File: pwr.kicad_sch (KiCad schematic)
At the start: 52 parts, among them U1 STM32N657X0H3Q

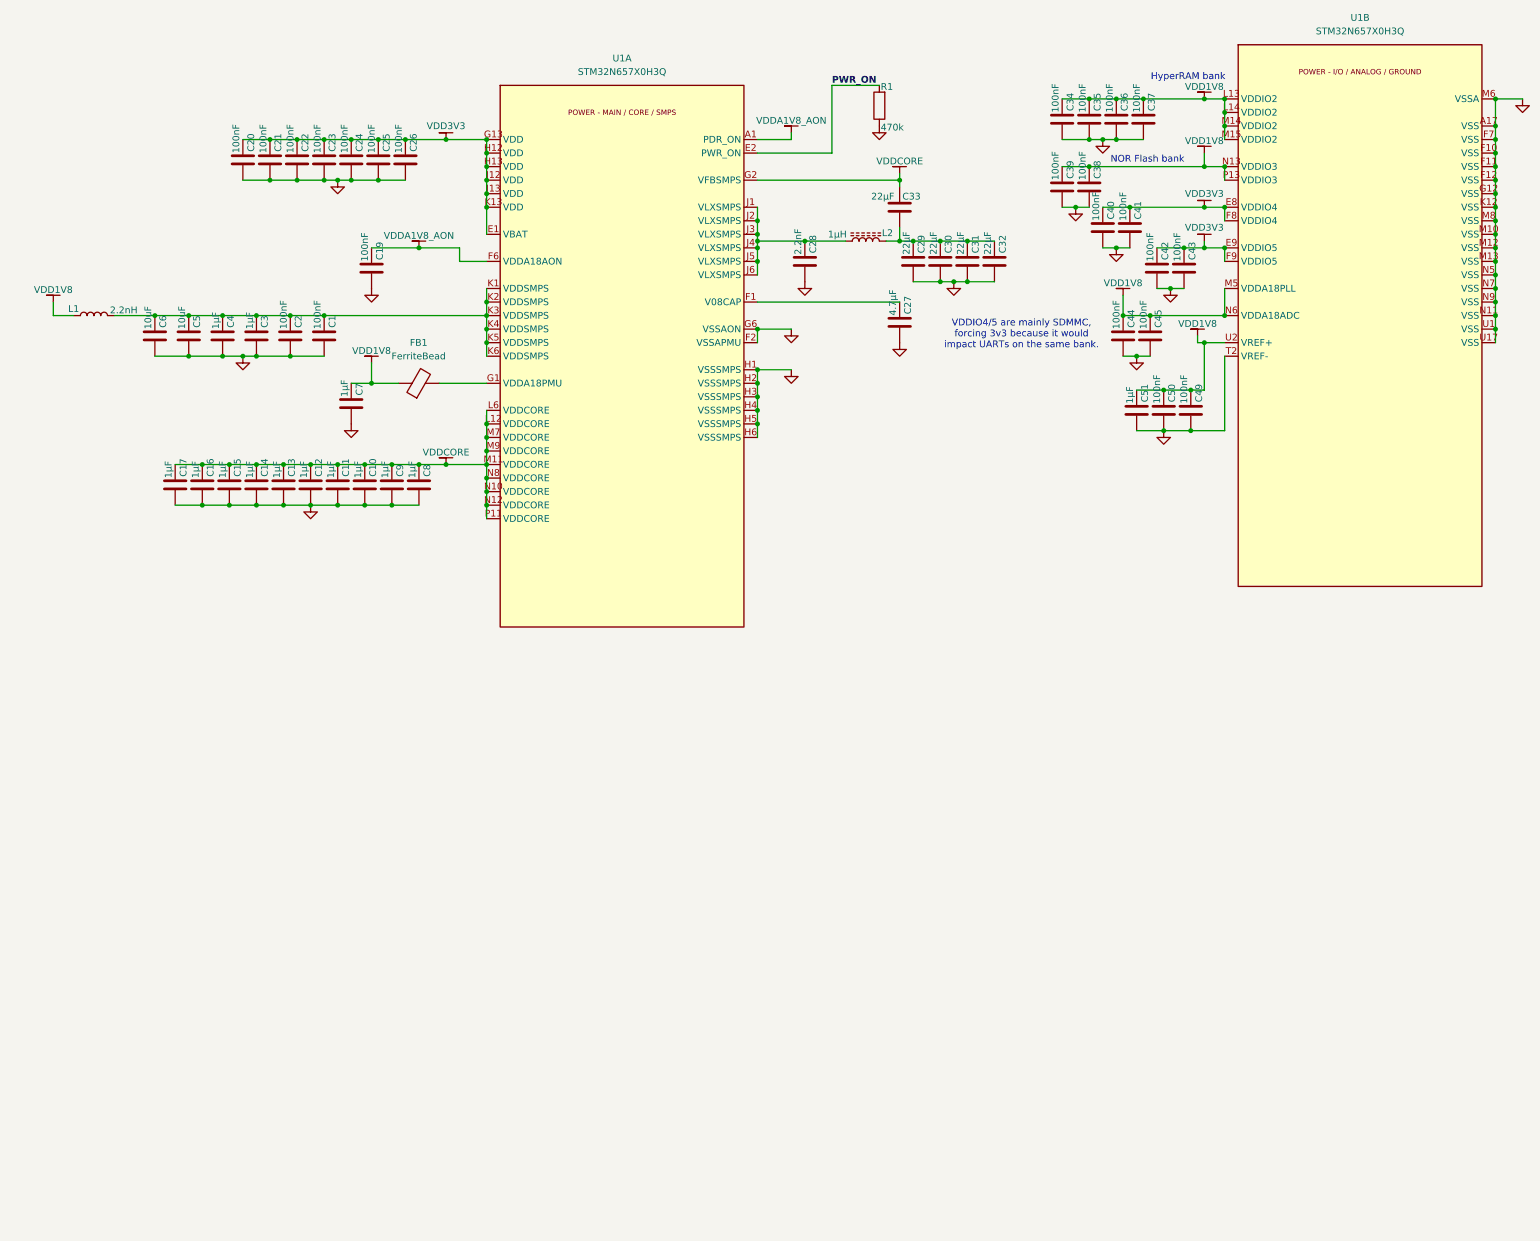
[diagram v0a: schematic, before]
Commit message: Power should be OK, memory & clk routing WIP
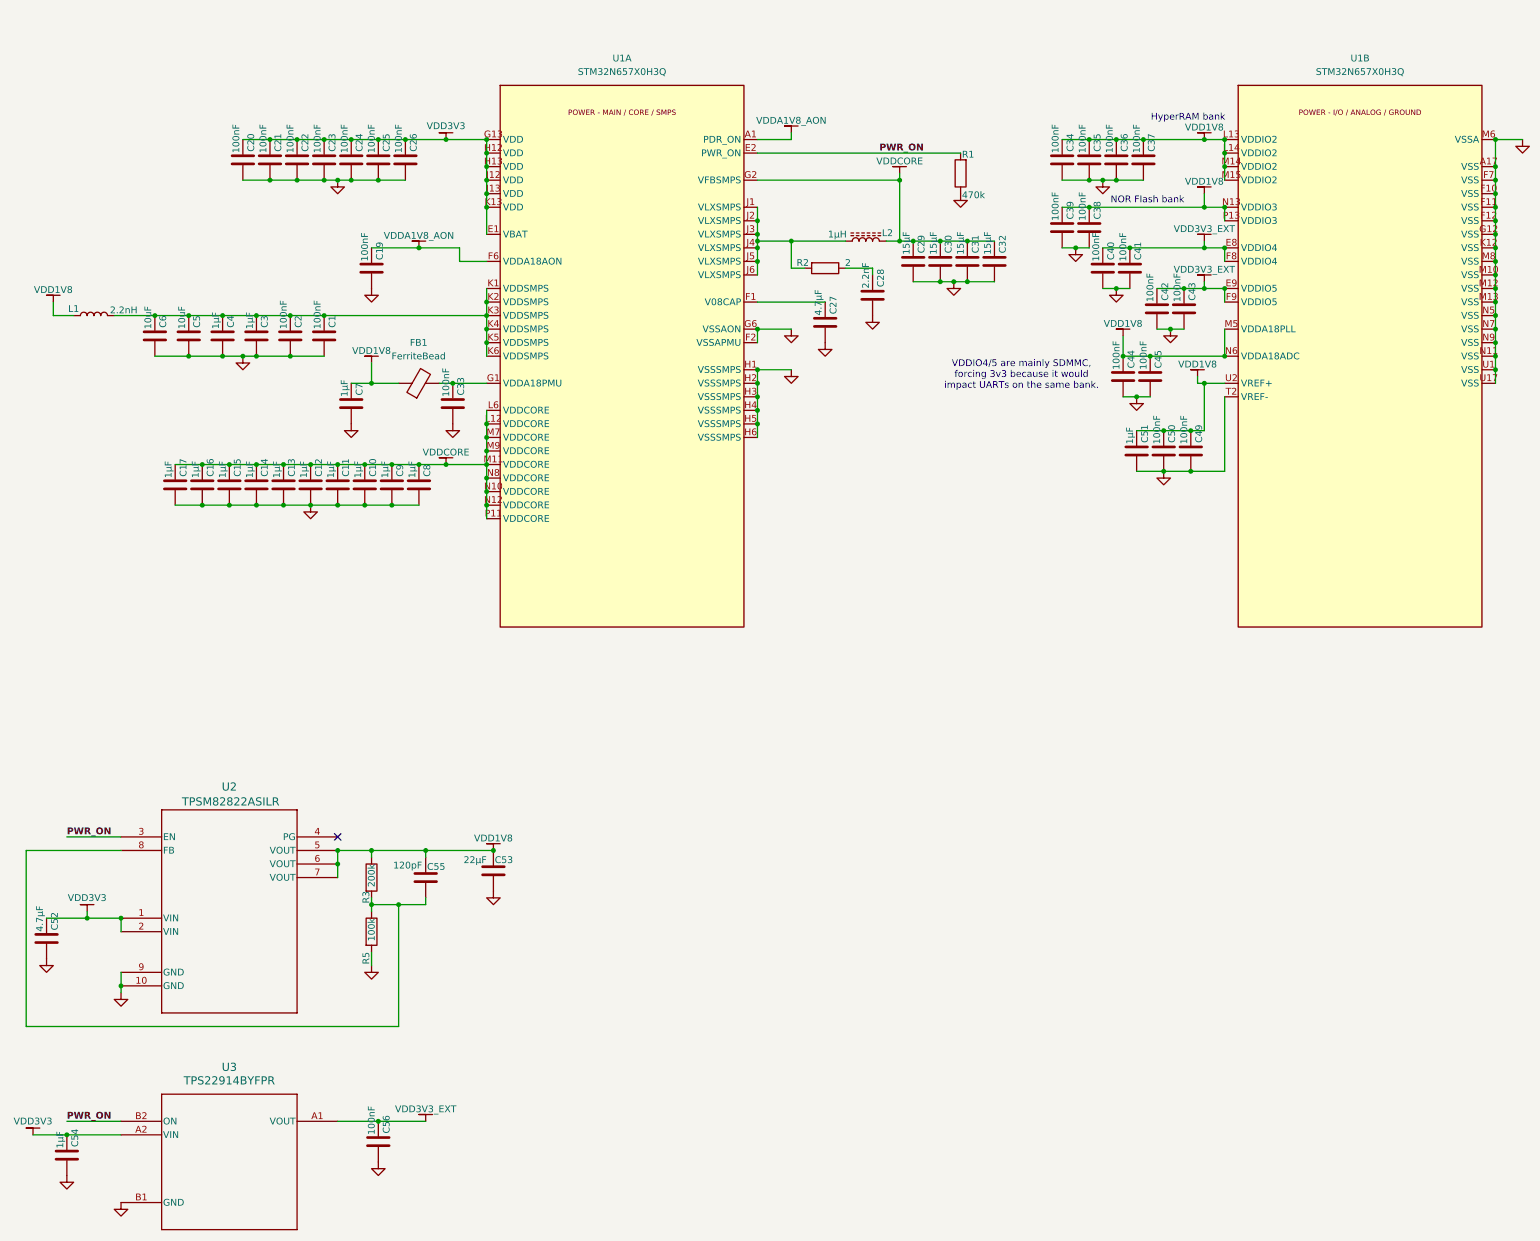
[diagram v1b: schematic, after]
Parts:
- added C52: 4.7µF, symbol Device:C
- added C53: 22µF, symbol Device:C
- added C54: 1µF, symbol Device:C
- added C55: 120pF, symbol Device:C
- added C56: 100nF, symbol Device:C
- added R2: 2, symbol Device:R
- added R3: 200k, symbol Device:R
- added R5: 100k, symbol Device:R
- added U2: TPSM82822ASILR, PLib:SIL0010D_TEX, symbol PLib:TPSM82822ASILR
- added U3: TPS22914BYFPR, PLib:YFP4_TEX, symbol PLib:TPS22914BYFPR
- C29, C30, C31, C32: value 22µF -> 15µF
- C33: value 22µF -> 100nF
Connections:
- net GND: now also C33.2, C52.2, C53.2, C54.2, C56.2, R5.2, U2.10 (GND), U2.9 (GND), U3.B1 (GND)
- net PWR_ON: now also U2.3 (EN), U3.B2 (ON)
- net VDD1V8: now also C53.1, C55.1, R3.1, U2.5 (VOUT), U2.6 (VOUT), U2.7 (VOUT)
- net VDD3V3: now also C52.1, C54.1, U2.1 (VIN), U2.2 (VIN), U3.A2 (VIN); no longer C40.1, C41.1, C42.1, C43.1, U1.E8 (VDDIO4), U1.E9 (VDDIO5), U1.F8 (VDDIO4), U1.F9 (VDDIO5)
- net VDDCORE: now also C29.1, C30.1, C31.1, C32.1, L2.2; no longer C33.1
- net at FB1.2, U1.G1 (VDDA18PMU): now also C33.1
- net at L2.1, U1.J1 (VLXSMPS), U1.J2 (VLXSMPS)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: now also R2.2; no longer C28.1
- new net: C55.2, R3.2, R5.1, U2.8 (FB)
- new net: C28.1, R2.1
- new net VDD3V3_EXT: C40.1, C41.1, C42.1, C43.1, C56.1, U1.E8 (VDDIO4), U1.E9 (VDDIO5), U1.F8 (VDDIO4), U1.F9 (VDDIO5), U3.A1 (VOUT)
- no-connect marks 0 -> 1
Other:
- moved on the sheet: C27, C34, C35, C36, C37, C38, C39, C40, C41, C42, C43, C44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

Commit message: Lots of footprint & memory schematic
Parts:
- removed C1, C42, C43, C44, C45, C49, C50: 100nF, symbol Device:C
- removed C10, C11, C12, C13, C14, C15, C16, C7, C8, C9: 1µF, symbol Device:C
- added C69, C70, C71, C72, C73, C74, C75, C76, C77, C78, C79, C80, C81, C82, C83: 100nF, Capacitor_SMD:C_0201_0603Metric, symbol Device:C
- C17, C2, C20, C21, C22, C23, C24, C25, C26, C4, C51: footprint (none) -> Capacitor_SMD:C_0201_0603Metric
- C19: value 100nF -> 10uF; footprint (none) -> Capacitor_SMD:C_0402_1005Metric
- C27, C28, C54, C56, C6: footprint (none) -> Capacitor_SMD:C_0402_1005Metric
- C29, C30, C31, C32, C52, C53, C55, FB1, L1: footprint (none) -> Capacitor_SMD:C_0603_1608Metric
- C3: value 1µF -> 100nF; footprint (none) -> Capacitor_SMD:C_0201_0603Metric
- C33, C34, C35, C36, C37, C38, C39, C40, C41: value 100nF -> 1µF; footprint (none) -> Capacitor_SMD:C_0201_0603Metric
- C5: value 10uF -> 1µF; footprint (none) -> Capacitor_SMD:C_0201_0603Metric
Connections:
- net GND: now also C69.2, C70.2, C71.2, C72.2, C73.2, C74.2, C75.2, C76.2, C77.2, C78.2, C79.2, C80.2, C81.2, C82.2, C83.2
- net VDD1V8: now also C71.1, C72.1, C73.1, C74.1, C75.1, C76.1, C81.1, C82.1, C83.1; no longer C34.1, C35.1, C36.1, C37.1, C38.1, C39.1
- net VDD3V3_EXT: now also C77.1, C78.1, C79.1, C80.1; no longer C40.1, C41.1
- net VDDA1V8_AON: now also C69.1; no longer C19.1
- net VDDCORE: now also C33.1, C34.1, C35.1, C36.1, C37.1, C38.1, C39.1, C40.1, C41.1
- net at C2.1, C3.1, C4.1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: now also C19.1
- net at FB1.2, U1.G1 (VDDA18PMU): now also C70.1; no longer C33.1
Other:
- note added: "VDDIO2 bank: PO[5:0] and PP[15:0] VDDIO3 bank: PN[12:0]"

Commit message: Power & memory should be ok, sanity check in progress, routing started (routing first then GPIO set for mezzanine)
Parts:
- added C57, C58: 1µF, Capacitor_SMD:C_0402_1005Metric, symbol Device:C
- added U6: (no value), PLib:DQN_X2SON4_1mmx1mm, symbol PLib:TLV74018PDQNR
- U1: footprint C42418080:BGA-264_L14.0-W14.0-STM32N657X0H3Q -> SamacSys:BGA264C80P17X17_1400X1400X100
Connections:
- net GND: now also C57.2, C58.2, U6.2 (GND), U6.5 (THERM)
- net VDD3V3: now also C57.1, U6.3 (EN), U6.4 (IN)
- net VDDA1V8_AON: now also C58.1, U6.1 (OUT)

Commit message: All components placed, pwr decoupling routing in progress
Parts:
- removed C17: 1µF, Capacitor_SMD:C_0201_0603Metric, symbol Device:C
- removed L2: 1µH, symbol Device:L_Ferrite
- added L3: 1µH, Capacitor_SMD:C_0805_2012Metric, symbol Device:L
- FB1: footprint Capacitor_SMD:C_0603_1608Metric -> Inductor_SMD:L_0201_0603Metric; LCSC (none) -> C3032750
- R1: footprint (none) -> Resistor_SMD:R_0402_1005Metric; LCSC (none) -> C25790
- R2, R3, R5: footprint (none) -> Resistor_SMD:R_0402_1005Metric
- U2: value TPSM82822ASILR -> TPSM82823ASILR
- U3: value TPS22914BYFPR -> TPS22915BYFPR; LCSC C1848394 -> C478464
- U6: LCSC (none) -> C3744287
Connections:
- net VDDCORE: now also L3.2
- net at R2.2, U1.J1 (VLXSMPS), U1.J2 (VLXSMPS)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: now also L3.1
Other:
- note added: "Both have quick discharge to respect pwr down seq"
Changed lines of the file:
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@@
 		)
 	)
+	(text "Both have quick discharge to respect pwr down seq"
+		(exclude_from_sim no)
+		(at 77.978 216.916 0)
+		(effects
+			(font
+				(size 1.27 1.27)
+			)
+		)
+	)
 	(text "VDDIO4/5 are mainly SDMMC,\nforcing 3v3 because it would\nimpact UARTs on the same bank."
 		(exclude_from_sim no)
@@
 	)
 	(junction
-		(at 72.39 107.95)
-		(diameter 0)
-		(color 0 0 0 0)
-	)
-	(junction
 		(at 125.73 54.61)
 		(diameter 0)
@@
 	)
 	(junction
-		(at 72.39 115.57)
-		(diameter 0)
-		(color 0 0 0 0)
-	)
-	(junction
 		(at 85.09 54.61)
 		(diameter 0)
@@
 	(wire
 		(pts
-			(xy 67.31 115.57) (xy 72.39 115.57)
-		)
-		(stroke
-			(width 0)
-			(type default)
-		)
-	)
-	(wire
-		(pts
 			(xy 125.73 52.07) (xy 125.73 49.53)
 		)
@@
 	(wire
 		(pts
-			(xy 67.31 107.95) (xy 72.39 107.95)
-		)
-		(stroke
-			(width 0)
-			(type default)
-		)
-	)
-	(wire
-		(pts
 			(xy 200.66 66.04) (xy 203.2 66.04)
 		)
@@
 			)
 		)
-		(property "Value" "TPS22914BYFPR"
+		(property "Value" "TPS22915BYFPR"
 			(at 77.47 223.52 0)
 			(show_name no)
@@
 			)
 		)
-		(property "Datasheet" "https://www.ti.com/lit/gpn/tps22914"
+		(property "Datasheet" "https://www.ti.com/lit/gpn/tps22915"
 			(at 57.15 231.14 0)
 			(hide yes)
@@
 			)
 		)
-		(property "Description" ""
+		(property "Description" "Need TPS22915 to have quick discharge"
 			(at 57.15 231.14 0)
 			(hide yes)
@@
 			)
 		)
-		(property "LCSC" "C1848394"
+		(property "LCSC" "C478464"
 			(at 57.15 231.14 0)
 			(hide yes)
@@
 	(symbol
 		(lib_id "Device:C")
-		(at 67.31 111.76 0)
-		(unit 1)
-		(body_style 1)
-		(exclude_from_sim no)
-		(in_bom yes)
-		(on_board yes)
-		(in_pos_files yes)
-		(dnp no)
-		(property "Reference" "C17"
-			(at 68.834 110.236 90)
-			(show_name no)
-			(do_not_autoplace no)
-			(effects
-				(font
-					(size 1.27 1.27)
-				)
-				(justify left)
-			)
-		)
-		(property "Value" "1µF"
-			(at 66.04 110.49 90)
-			(show_name no)
-			(do_not_autoplace no)
-			(effects
-				(font
-					(size 1.27 1.27)
-				)
-				(justify left)
-			)
-		)
-		(property "Footprint" "Capacitor_SMD:C_0201_0603Metric"
-			(at 68.2752 115.57 0)
-			(hide yes)
-			(show_name no)
-			(do_not_autoplace no)
-			(effects
-				(font
-					(size 1.27 1.27)
-				)
-			)
-		)
-		(property "Datasheet" ""
-			(at 67.31 111.76 0)
-			(hide yes)
-			(show_name no)
-			(do_not_autoplace no)
-			(effects
-				(font
-					(size 1.27 1.27)
-				)
-			)
-		)
-		(property "Description" "Unpolarized capacitor"
-			(at 67.31 111.76 0)
-			(hide yes)
-			(show_name no)
-			(do_not_autoplace no)
-			(effects
-				(font
-					(size 1.27 1.27)
-				)
-			)
-		)
-		(pin "1"
-		)
-		(pin "2"
-		)
-		(instances
-			(project "STM32N6_SOM"
-				(path "/af5ed896-0f4b-4a3b-83a3-1b3549d508f8/b069fc75-800d-4bb3-9535-5aba8669997e"
-					(reference "C17")
-					(unit 1)
-				)
-			)
-		)
-	)
-	(symbol
-		(lib_id "Device:C")
 		(at 110.49 50.8 0)
 		(unit 1)
@@
 			)
 		)
-		(property "Footprint" ""
+		(property "Footprint" "Resistor_SMD:R_0402_1005Metric"
 			(at 102.362 185.42 90)
 			(hide yes)
@@
 			)
 		)
-		(property "Footprint" ""
+		(property "Footprint" "Resistor_SMD:R_0402_1005Metric"
 			(at 189.23 69.342 90)
 			(hide yes)
@@
 			)
 		)
+		(property "LCSC" "C3744287"
+			(at 157.48 232.41 0)
+			(hide yes)
+			(show_name no)
+			(do_not_autoplace no)
+			(effects
+				(font
+					(size 1.27 1.27)
+				)
+			)
+		)
 		(pin "5"
 		)
@@
 	)
 	(symbol
-		(lib_id "Device:L_Ferrite")
-		(at 196.85 66.04 90)
+		(lib_id "power:GND")
+		(at 213.36 73.66 0)
 		(unit 1)
 		(body_style 1)
@@
 		(in_pos_files yes)
 		(dnp no)
-		(property "Reference" "L2"
-			(at 200.914 64.516 90)
+		(fields_autoplaced yes)
+		(property "Reference" "#PWR016"
+			(at 213.36 80.01 0)
+			(hide yes)
 			(show_name no)
 			(do_not_autoplace no)
@@
 			)
 		)
-		(property "Value" "1µH"
-			(at 191.516 64.77 90)
+		(property "Value" "GND"
+			(at 213.36 78.74 0)
+			(hide yes)
 			(show_name no)
 			(do_not_autoplace no)
@@
 		)
 		(property "Footprint" ""
-			(at 196.85 66.04 0)
+			(at 213.36 73.66 0)
 			(hide yes)
 			(show_name no)
@@
 		)
 		(property "Datasheet" ""
-			(at 196.85 66.04 0)
+			(at 213.36 73.66 0)
 			(hide yes)
 			(show_name no)
@@
 			)
 		)
-		(property "Description" "Inductor with ferrite core"
-			(at 196.85 66.04 0)
+		(property "Description" "Power symbol creates a global label with name \"GND\" , ground"
+			(at 213.36 73.66 0)
 			(hide yes)
 			(show_name no)
@@
 		(pin "1"
 		)
-		(pin "2"
-		)
 		(instances
 			(project "STM32N6_SOM"
 				(path "/af5ed896-0f4b-4a3b-83a3-1b3549d508f8/b069fc75-800d-4bb3-9535-5aba8669997e"
-					(reference "L2")
+					(reference "#PWR016")
 					(unit 1)
 				)
@@
 	)
 	(symbol
-		(lib_id "power:GND")
-		(at 213.36 73.66 0)
+		(lib_id "Device:L")
+		(at 196.85 66.04 90)
 		(unit 1)
 		(body_style 1)
@@
 		(dnp no)
 		(fields_autoplaced yes)
-		(property "Reference" "#PWR016"
-			(at 213.36 80.01 0)
-			(hide yes)
+		(property "Reference" "L3"
+			(at 196.85 60.96 90)
 			(show_name no)
 			(do_not_autoplace no)
@@
 			)
 		)
-		(property "Value" "GND"
-			(at 213.36 78.74 0)
-			(hide yes)
+		(property "Value" "1µH"
+			(at 196.85 63.5 90)
 			(show_name no)
 			(do_not_autoplace no)
@@
 			)
 		)
-		(property "Footprint" ""
-			(at 213.36 73.66 0)
+		(property "Footprint" "Capacitor_SMD:C_0805_2012Metric"
+			(at 196.85 66.04 0)
 			(hide yes)
 			(show_name no)
@@
 		)
 		(property "Datasheet" ""
-			(at 213.36 73.66 0)
+			(at 196.85 66.04 0)
 			(hide yes)
 			(show_name no)
@@
 			)
 		)
-		(property "Description" "Power symbol creates a global label with name \"GND\" , ground"
-			(at 213.36 73.66 0)
+		(property "Description" "Inductor"
+			(at 196.85 66.04 0)
+			(hide yes)
+			(show_name no)
+			(do_not_autoplace no)
+			(effects
+				(font
+					(size 1.27 1.27)
+				)
+			)
+		)
+		(property "LCSC" "C1042"
+			(at 196.85 66.04 90)
 			(hide yes)
 			(show_name no)
@@
 		(pin "1"
 		)
+		(pin "2"
+		)
 		(instances
 			(project "STM32N6_SOM"
 				(path "/af5ed896-0f4b-4a3b-83a3-1b3549d508f8/b069fc75-800d-4bb3-9535-5aba8669997e"
-					(reference "#PWR016")
+					(reference "L3")
 					(unit 1)
 				)
@@
 			)
 		)
-		(property "Value" "TPSM82822ASILR"
+		(property "Value" "TPSM82823ASILR"
 			(at 77.724 171.196 0)
 			(show_name no)
@@
 			)
 		)
-		(property "Datasheet" "https://www.ti.com/lit/gpn/tpsm82822a"
+		(property "Datasheet" "https://www.ti.com/lit/gpn/tpsm82823a"
 			(at 57.15 177.8 0)
 			(hide yes)
@@
 			)
 		)
-		(property "Footprint" ""
+		(property "Footprint" "Resistor_SMD:R_0402_1005Metric"
 			(at 102.362 195.58 90)
 			(hide yes)
@@
 			)
 		)
-		(property "Footprint" "Capacitor_SMD:C_0603_1608Metric"
+		(property "Footprint" "Inductor_SMD:L_0201_0603Metric"
 			(at 113.03 94.488 90)
 			(hide yes)
@@
 			)
 		)
-		(property "Description" "Ferrite bead 18R @ 100MHz 750mA"
+		(property "Description" "Ferrite bead 19R @ 100MHz 6A 10mOhm"
 			(at 113.03 92.71 0)
 			(hide yes)
@@
 			)
 		)
+		(property "LCSC" "C3032750"
+			(at 113.03 92.71 90)
+			(hide yes)
+			(show_name no)
+			(do_not_autoplace no)
+			(effects
+				(font
+					(size 1.27 1.27)
+				)
+			)
+		)
 		(pin "2"
 		)
@@
 			)
 		)
-		(property "Footprint" ""
+		(property "Footprint" "Resistor_SMD:R_0402_1005Metric"
 			(at 216.408 53.34 90)
 			(hide yes)
@@
 			(at 214.63 53.34 0)
 			(hide yes)
+			(show_name no)
+			(do_not_autoplace no)
+			(effects
+				(font
+					(size 1.27 1.27)
+				)
+			)
+		)
+		(property "LCSC" "C25790"
+			(at 214.63 53.34 0)
+			(hide yes)

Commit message: Power decoupling done, will work on pwr supplies next then connector routing
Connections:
- net VDD1V8: now also L1.2; no longer L1.1
- net VDDCORE: now also L3.1; no longer L3.2
- net at C19.1, C2.1, C3.1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: now also L1.1; no longer L1.2
- net at R2.2, U1.J1 (VLXSMPS), U1.J2 (VLXSMPS)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: now also L3.2; no longer L3.1
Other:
- moved on the sheet: L1, L3
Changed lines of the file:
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@@
 	(symbol
 		(lib_id "Device:L")
-		(at 52.07 80.01 90)
+		(at 52.07 80.01 270)
+		(mirror x)
 		(unit 1)
 		(body_style 1)
@@
 		(dnp no)
 		(property "Reference" "L1"
-			(at 48.26 78.74 90)
+			(at 55.88 78.74 90)
 			(show_name no)
 			(do_not_autoplace no)
@@
 		)
 		(property "Value" "2.2nH"
-			(at 57.658 78.994 90)
+			(at 46.482 78.994 90)
 			(show_name no)
 			(do_not_autoplace no)
@@
 	(symbol
 		(lib_id "Device:L")
-		(at 196.85 66.04 90)
+		(at 196.85 66.04 270)
+		(mirror x)
 		(unit 1)
 		(body_style 1)
@@
 		(in_pos_files yes)
 		(dnp no)
-		(fields_autoplaced yes)
 		(property "Reference" "L3"
 			(at 196.85 60.96 90)
